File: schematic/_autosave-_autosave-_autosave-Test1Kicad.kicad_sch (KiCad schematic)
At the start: 73 parts, among them IC1 BMI055, J1 Power Module 1, J10 CAP & ADC IN, J11 SPI Port, J12 I2C A, J13 FMU PWM OUT, J14 PPM RC, J15 2908-05WB-MG, J16 RC, J17 SBUS, J2 Power Module 2, J3 USB, J4 Telemetry 1, J5 Telemetry 2, J6 UART & I2C B, J7 CAN 1, J8 CAN 2, J9 GPS Module, U1 STM32F765IIKx, U10 TJA1051TK-3, U11 LT3080xDD, U12 LP5907MFX-3.3, U3 IST8310, U4 ICM-20602, U5 ICM-20689, U6 MS5611-01BA, U8 STM32F103V8Tx, U9 TJA1051TK-3, Y1 ABM2-8.000MHZ-D4Y-T

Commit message: IO/PWM port, cleaned up FMU PXIO connections
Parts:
- removed D1: LED, symbol Device:LED
- removed J16: RC, symbol Connector:Conn_01x05_Socket
- removed LS1: PS1240P02BT, PS1240P02BT:XDCR_PS1240P02BT, symbol PS1240P02BT:PS1240P02BT
- removed R1: 10K, symbol Device:R
- removed R5: 68, symbol Device:R
- added J18: IO/PWM out, symbol Connector:Conn_01x10_Socket
- C14, C15: value 22pF -> 18pF
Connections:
- net ADC1_SPARE_1 (3.3V): now also U8.34 (PC5); no longer U1.N5 (PC4)
- net ADC1_SPARE_2 (6.6V): now also U8.33 (PC4); no longer U1.N4 (PA4)
- net BAT1_I: no longer U8.24 (PA1)
- net BAT1_V: no longer U8.23 (PA0)
- net BAT2_I: no longer U8.26 (PA3)
- net BAT2_V: no longer U8.25 (PA2)
- net FMU_CAP1: now also U8.31 (PA6); no longer U1.P4 (PA5)
- net FMU_CAP2: now also U8.32 (PA7); no longer U1.A10 (PB3)
- net FMU_CAP3: now also U8.35 (PB0); no longer U1.R13 (PB11)
- net GND: now also J18.10 (Pin_10)
- net RC_INPUT (aka PPM_IN): now also U8.36 (PB1); no longer U1.C4 (PI5)
- net RSSI_IN: now also U8.90 (PB4); no longer U1.R5 (PB0)
- net UART8_RX_PX4IO: now also U8.68 (PA9); no longer U8.35 (PB0)
- net UART8_TX_PX4IO: now also U8.69 (PA10); no longer U8.36 (PB1)
- net USART6_TX_TELEM3/(RC_INPUT): now also U8.89 (PB3); no longer U1.A7 (PG14)
- net VDD: no longer C10.2, C11.1, C2.2, C4.2, C6.2, C8.2, C9.1, IC1.11 (VDDIO), IC1.3 (VDD), J9.8 (Pin_8), U1.C5 (VDD), U3.13 (DVDD), U4.16 (VDD), U5.13 (VDD), U6.1 (VDD)
- net VDDIO: no longer C3.1, C7.1, U1.C7 (VDD), U4.1 (VDDIO), U5.8 (VDDIO)
- net VDD_3V3: no longer J17.2 (Pin_2)
- net VDD_ports: now reaches U1.C9 (VDD)
- net VDD_ports: now also J9.8 (Pin_8)
- net TIM1_CH1: now reaches J10.5 (Pin_5)
- net TIM1_CH1: now also U8.67 (PA8)
- net SBUS_OUT: now reaches U8.47 (PB10)
- net SBUS_OUT: now also J17.2 (Pin_2)
- net IO_CH1: now reaches U8.92 (PB6)
- net IO_CH1: now also J18.2 (Pin_2)
- net IO_CH2: now reaches U8.93 (PB7)
- net IO_CH2: now also J18.3 (Pin_3)
- net IO_CH3: now reaches U8.95 (PB8)
- net IO_CH3: now also J18.4 (Pin_4)
- net IO_CH4: now reaches U8.96 (PB9)
- net IO_CH4: now also J18.5 (Pin_5)
- new net IO_CH5: J18.6 (Pin_6), U8.23 (PA0)
- new net IO_CH6: J18.7 (Pin_7), U8.24 (PA1)
- new net IO_CH7: J18.8 (Pin_8), U8.25 (PA2)
- new net IO_CH8: J18.9 (Pin_9), U8.26 (PA3)
- new net VDDIO_sensors: C11.1, C3.1, C7.1, IC1.11 (VDDIO), U1.C7 (VDD), U4.1 (VDDIO), U5.8 (VDDIO)
- new net VDD_sensors: C10.2, C2.2, C4.2, C6.2, C8.2, C9.1, IC1.3 (VDD), U1.C5 (VDD), U3.13 (DVDD), U4.16 (VDD), U5.13 (VDD), U6.1 (VDD)
- no-connect marks 5 -> 6
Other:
- note added: "FMU CONNECTIONS"
- note added: "PXIO CONNECTIONS"
- note added: "why telem 3 used"
- note removed: "DSM/SBUS RC"
- moved on the sheet: C1, C10, C11, C12, C13, C14, C15, C18, C19, C2, C28, C29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

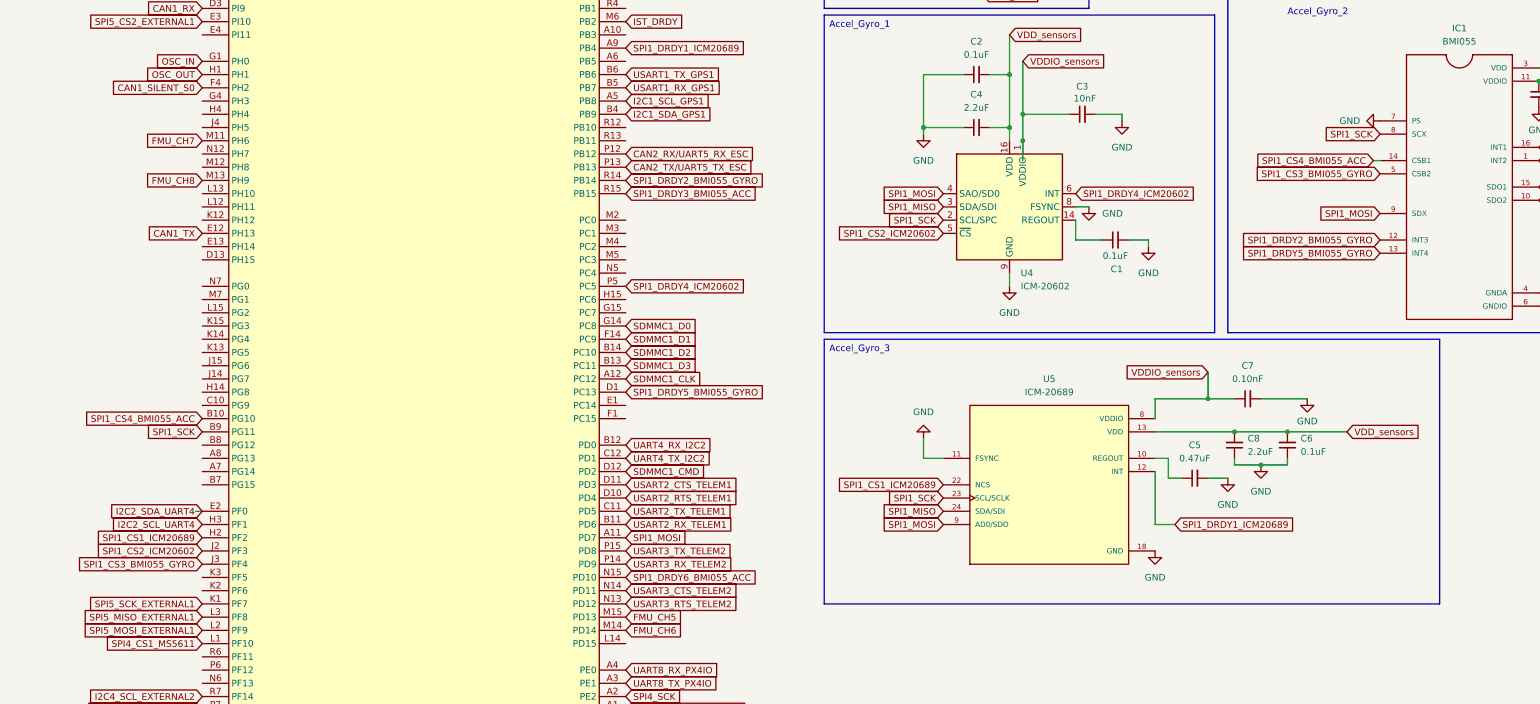
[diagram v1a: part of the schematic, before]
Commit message: CAN 2 silent connection
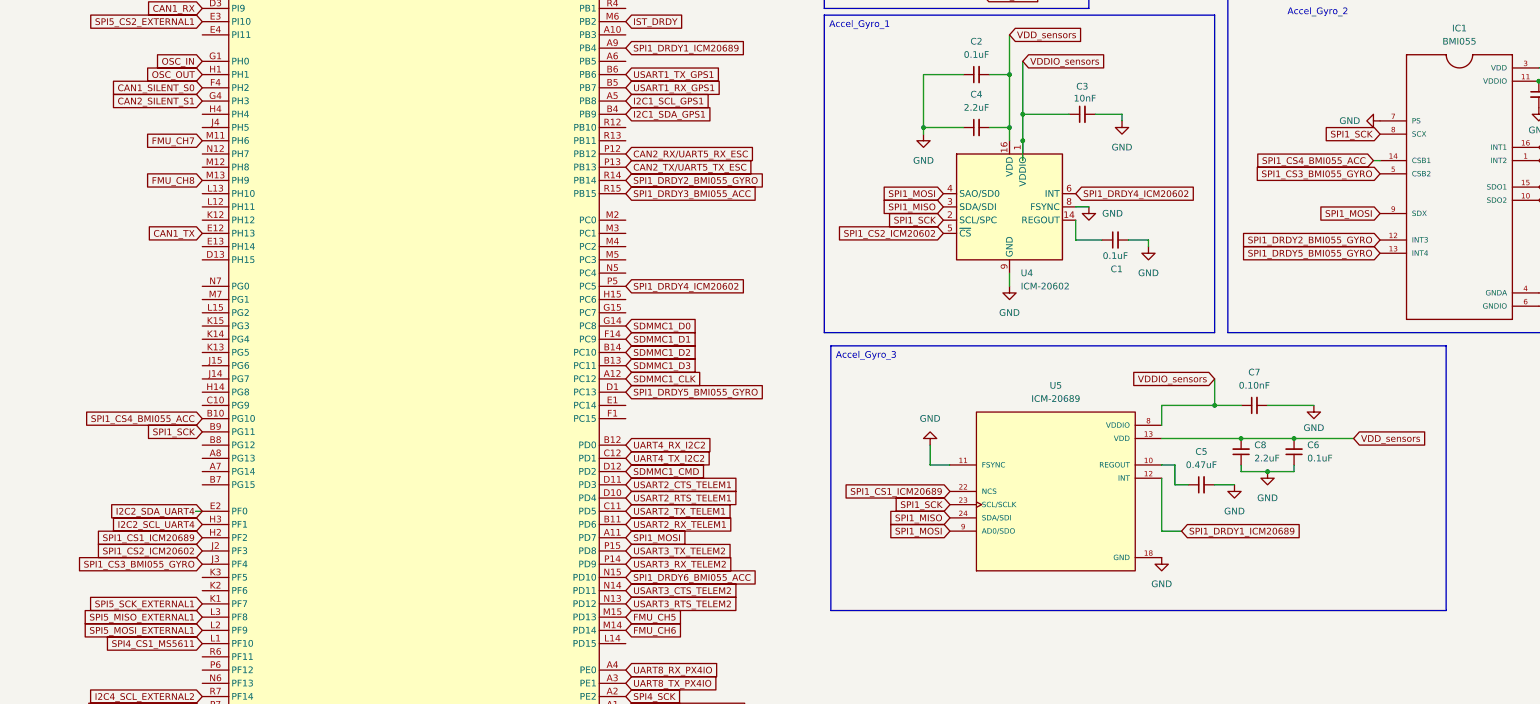
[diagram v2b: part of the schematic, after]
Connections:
- net CAN2_SILENT_S1: now also U1.G4 (PH3)
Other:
- moved on the sheet: C5, C6, C7, C8, U5

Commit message: DRC
fixed most errors 30 ish to go
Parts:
- added C16, C17: 100nF, symbol Device:C_Small
- added C30, C31: 1uf, symbol Device:C_Small
- added J16: RC, symbol Connector:Conn_01x05_Socket
- added R1: 10K, symbol Device:R
- added U13: LP5907MFX-3.3, Package_TO_SOT_SMD:SOT-23-5, symbol Regulator_Linear:LP5907MFX-3.3
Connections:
- net VDDA is gone; now on net VDD_3V3: C13.2, U3.2 (AVDD)
- net BMS_22.2V: now also C30.1, U13.1 (IN)
- net GND: now also U1.D5 (VSS), U1.D7 (VSS), U1.D8 (VSS), U1.D9 (VSS), U1.F10 (VSS), U1.F12 (VSS), U1.F13 (VCAP_2), U1.F2 (VSS), U1.F6 (VSS), U1.F7 (VSS), U1.F8 (VSS), U1.F9 (VSS), U1.G10 (VSS), U1.G12 (VSS), U1.G2 (VSS), U1.G6 (VSS), U1.G7 (VSS), U1.G8 (VSS), U1.G9 (VSS), U1.H10 (VSS), U1.H12 (VSS), U1.H6 (VSS), U1.H7 (VSS), U1.H8 (VSS), U1.H9 (VSS), U1.J10 (VSS), U1.J6 (VSS), U1.J7 (VSS), U1.J8 (VSS), U1.J9 (VSS), U1.K10 (VSS), U1.K6 (VSS), U1.K7 (VSS), U1.K8 (VSS), U1.K9 (VSS), U1.M1 (VSSA), U1.M10 (VCAP_1), U1.M8 (VSS), U1.M9 (VSS), U1.N1 (VREF-), U8.10 (VSS), U8.19 (VSSA), U8.20 (VREF-), U8.27 (VSS), U8.49 (VSS), U8.74 (VSS), U8.99 (VSS), C16.1, C16.2, C17.1, C17.2, C30.2, C31.2, J16.5 (Pin_5), U13.2 (GND)
- net OSC_IN: now also U8.12 (OSC_IN)
- net OSC_OUT: now also U8.13 (OSC_OUT)
- net RSSI_IN: now also R1.2
- net USART6_TX_TELEM3/(RC_INPUT): now also J16.2 (Pin_2)
- net VBUS: now also U1.H13 (VDDUSB)
- net VCC_5V: now also C31.1, J16.1 (Pin_1), U13.5 (OUT)
- net VDD_3V3: now also U1.F3 (VDD), U1.G13 (VDD), U1.G3 (VDD), U1.J12 (VDD), U1.J13 (VDD), U1.K4 (VDD), U1.N10 (VDD), U1.N8 (VDD), U1.N9 (VDD), U1.P1 (VREF+), U1.R1 (VDDA), U8.100 (VDD), U8.11 (VDD), U8.21 (VREF+), U8.22 (VDDA), U8.28 (VDD), U8.50 (VDD), U8.75 (VDD), J16.4 (Pin_4)
- net VDD_5V_RC_EN: now reaches U1.K13 (PG5)
- net VDD_5V_RC_EN: now also U13.3 (EN)
- net IST_RST: no longer names the net of U3.14 (~{RST})
- net VDD_3V3_SPEKTRUM_POWER_EN: no longer names the net of U8.3 (PE4)
- new net: J16.3 (Pin_3), R1.1
- no-connect marks 6 -> 129
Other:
- note added: "DSM/SBUS RC"
- note removed: "NOT CONNECTED"
